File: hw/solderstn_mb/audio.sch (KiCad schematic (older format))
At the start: 28 parts, among them J2103 CES-30207-158L120-67_Molex-Pi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, J2104 CES-703116-28PM_JST-conn, J2105 CES-30207-158L120-67_Molex-Pi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, J2106 CES-703116-28PM_JST-conn, U2102 TS4990IDT, U2103 TS4990IDT

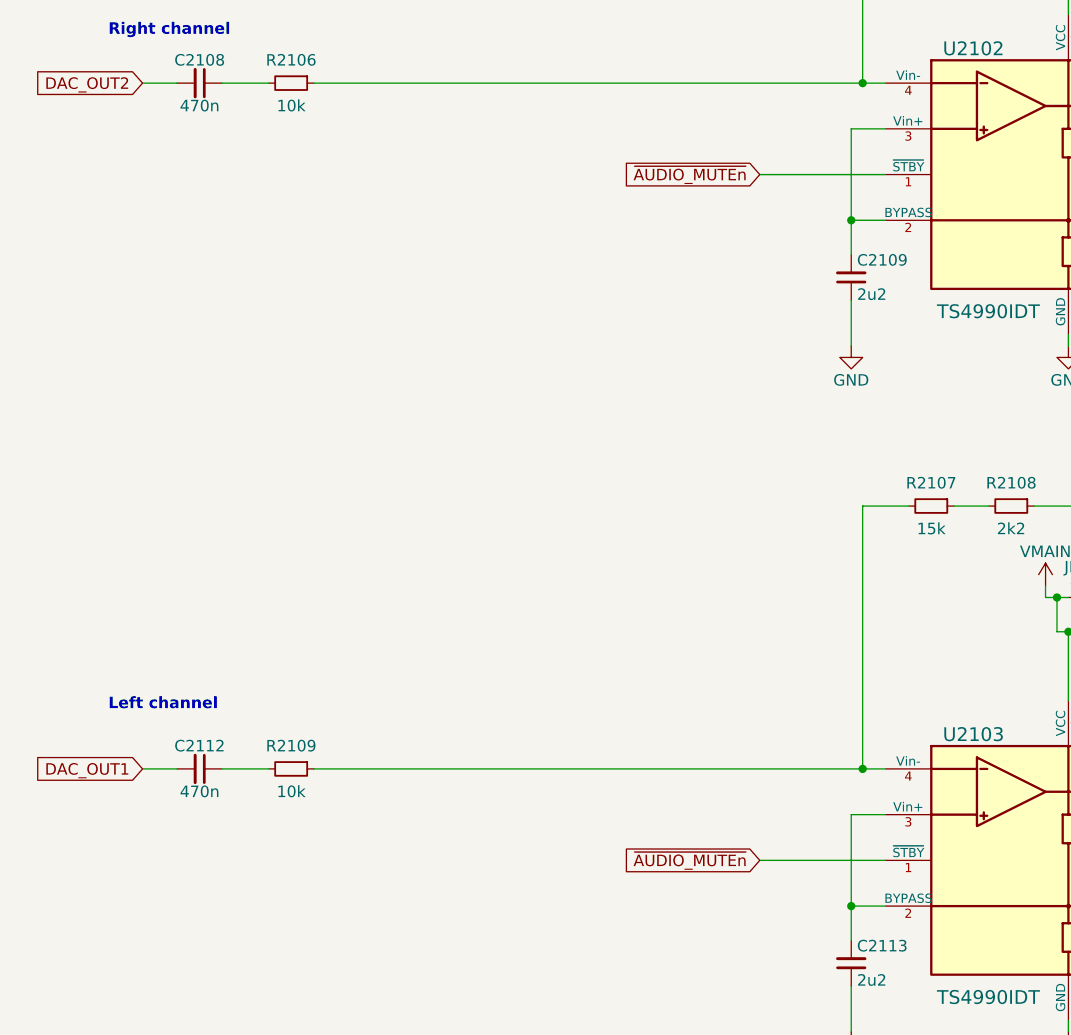
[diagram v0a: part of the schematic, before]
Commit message: MB: 1) remove 2x fan ctrls 2) MCU pin-out for a VS1063 3) add VS1063 DSP/codec to audio path (WIP)
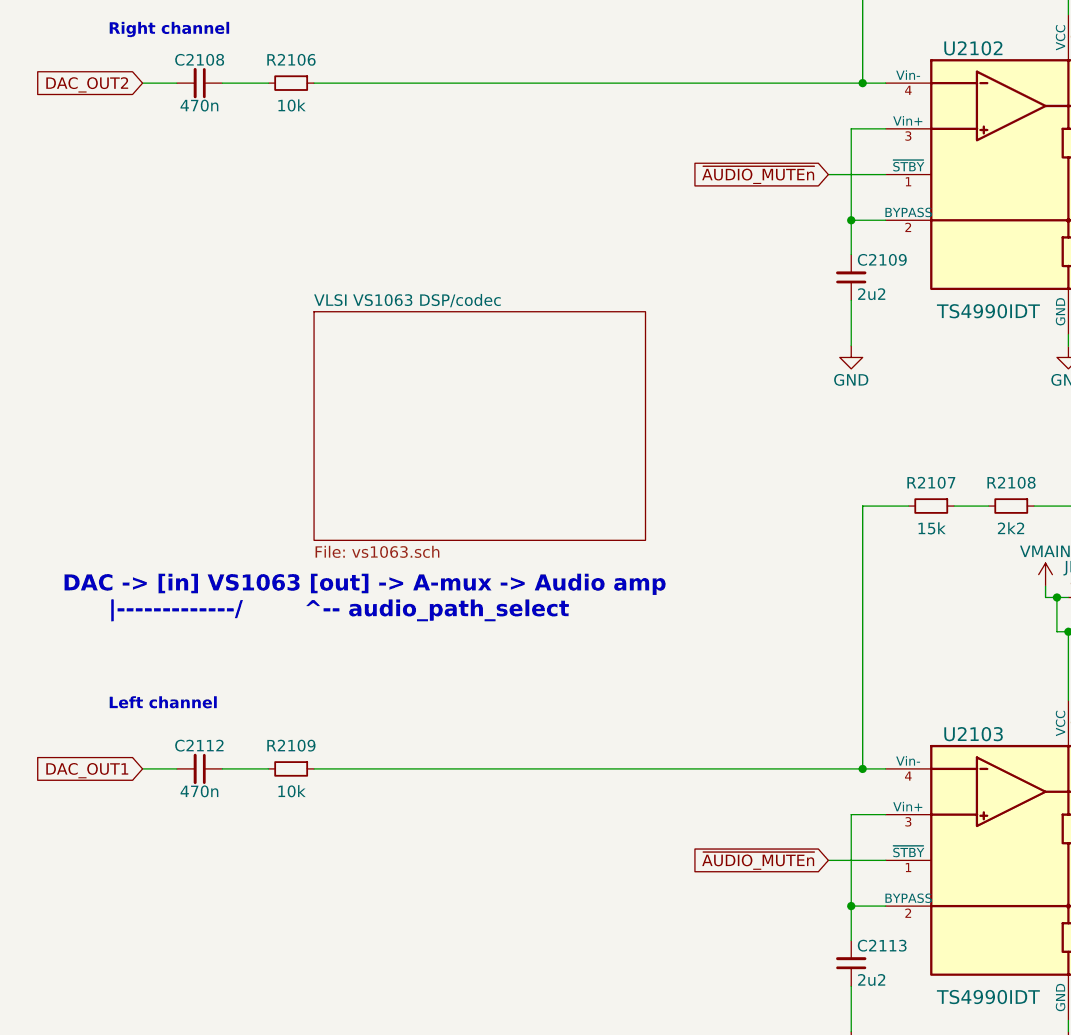
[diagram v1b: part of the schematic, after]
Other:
- note added: "DAC -> [in] VS1063 [out] -> A-mux -> Audio amp\n |-------------/ ^-- audio_path_select"
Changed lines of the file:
@@
 $Descr A4 11693 8268
 encoding utf-8
-Sheet 20 23
+Sheet 20 21
 Title "Audio & MP3/OGG/FLAC :)"
 Date "2020-11-04"
@@
 Connection ~ 4050 2700
 Wire Wire Line
-	4200 2500 3650 2500
-Text GLabel 3650 2500 0    50   Input ~ 0
+	4200 2500 3950 2500
+Text GLabel 3950 2500 0    50   Input ~ 0
 ~AUDIO_MUTEn~
 Text GLabel 950  2100 0    50   Input ~ 0
@@
 Connection ~ 4050 5700
 Wire Wire Line
-	4200 5500 3650 5500
-Text GLabel 3650 5500 0    50   Input ~ 0
+	4200 5500 3950 5500
+Text GLabel 3950 5500 0    50   Input ~ 0
 ~AUDIO_MUTEn~
 Text GLabel 950  5100 0    50   Input ~ 0
@@
 Wire Wire Line
 	4100 3950 4100 5100
+$Sheet
+S 1700 3100 1450 1000
+U 5FEE4431
+F0 "VLSI VS1063 DSP/codec" 50
+F1 "vs1063.sch" 50
+$EndSheet
+Text Notes 600  4450 0    70   ~ 14
+DAC -> [in] VS1063 [out] -> A-mux -> Audio amp\n      |-------------/        ^-- audio_path_select
 $EndSCHEMATC

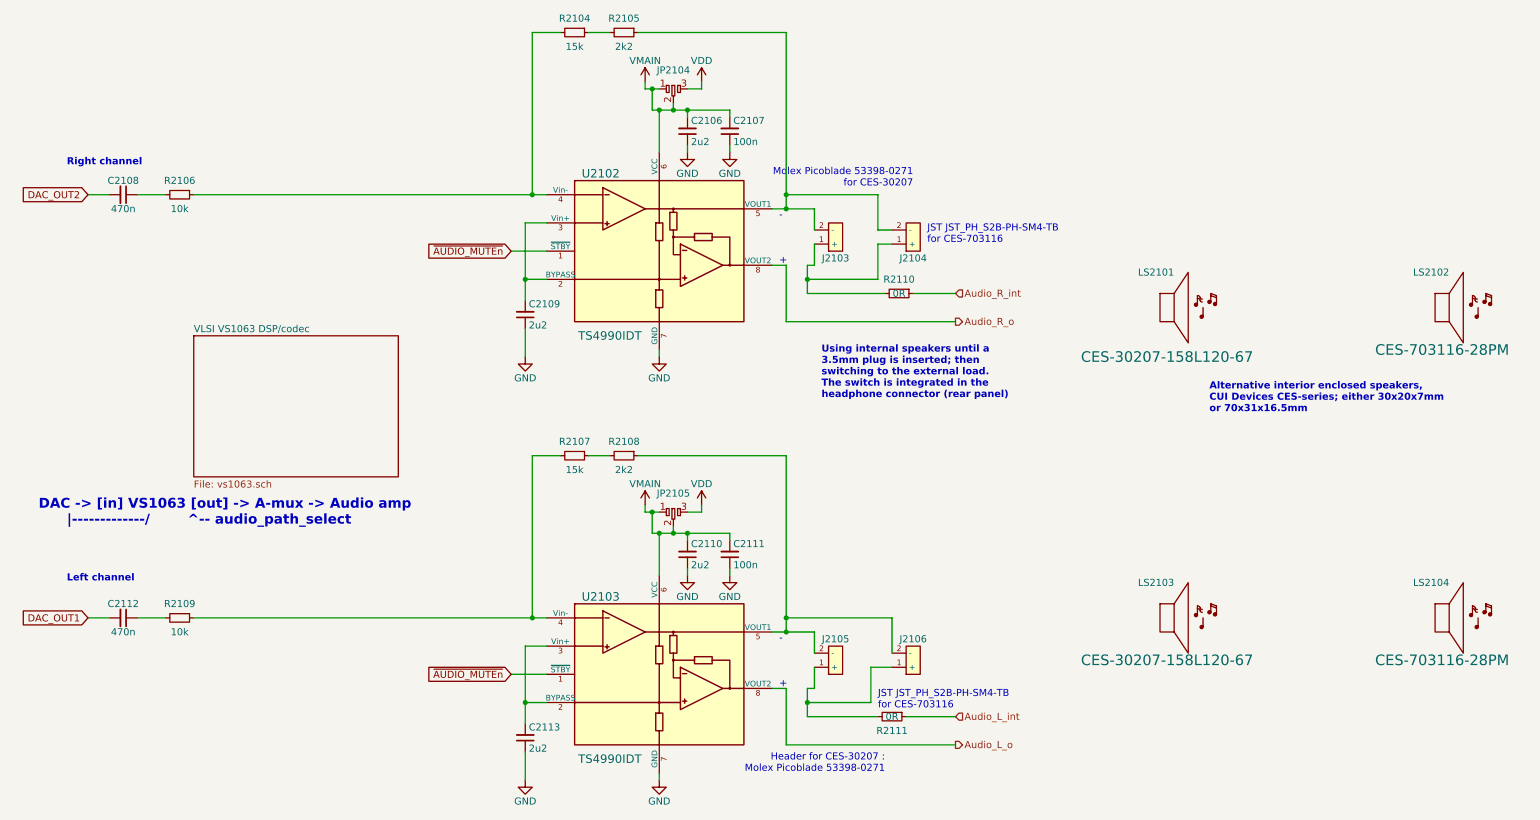
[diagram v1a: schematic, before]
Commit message: MB - Sch design: VS1063 in new audio path; Added: some new ESD, some fixups; Changes: some footprints, fixes
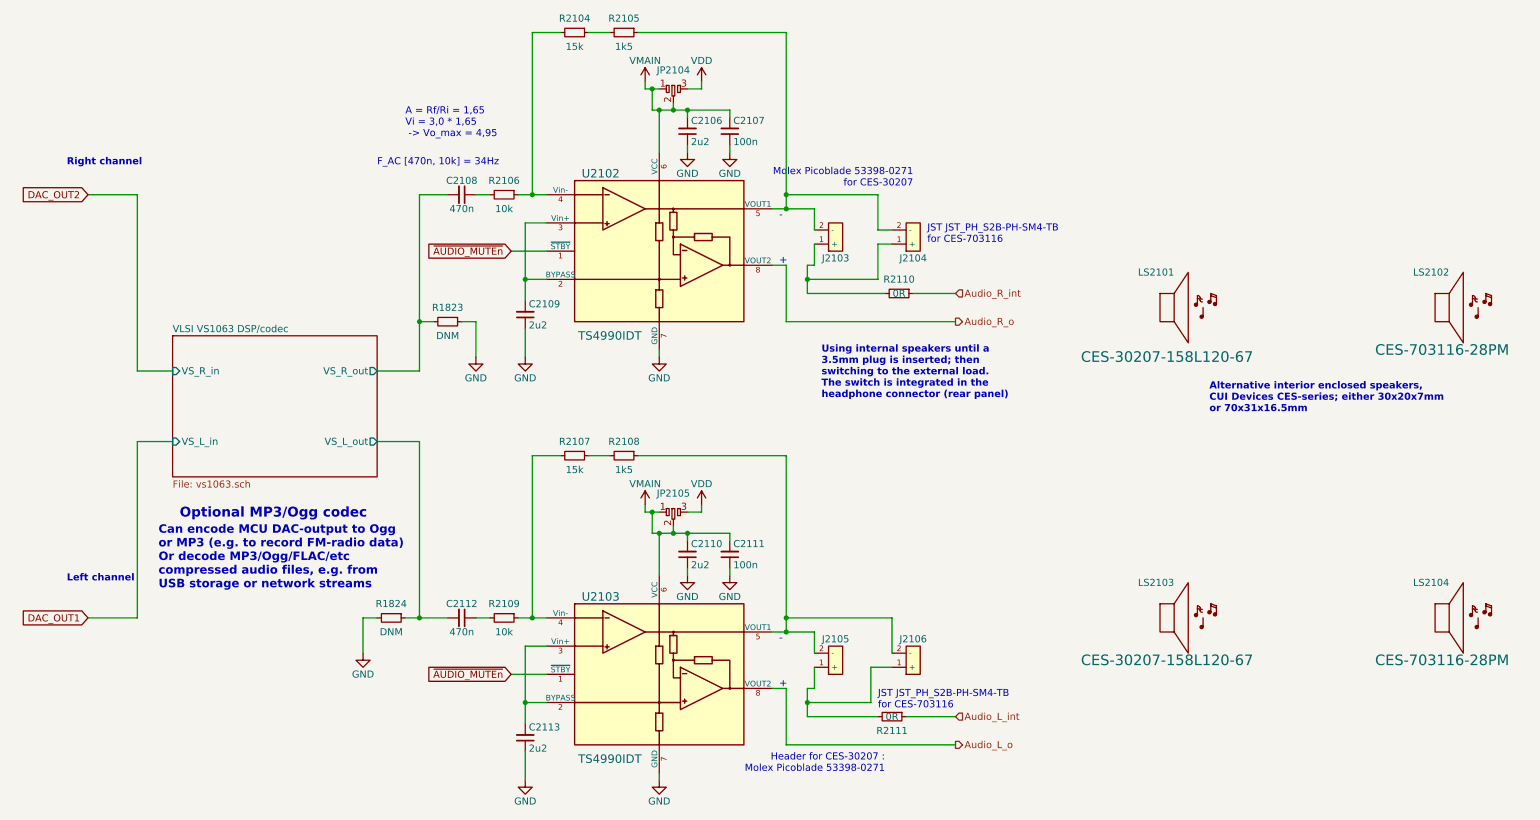
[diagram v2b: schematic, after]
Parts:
- added R1823, R1824: DNM, Resistor_SMD:R_0603_1608Metric, symbol Device:R_Small
- R2105, R2108: value 2k2 -> 1k5
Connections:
- net DAC_OUT1: no longer C2112.2
- net DAC_OUT2: no longer C2108.2
- net GND: now also R1823.1, R1824.2
- new net VLSI VS1063 DSP/codec/VS_L_out: C2112.2, R1824.1
- new net VLSI VS1063 DSP/codec/VS_R_out: C2108.2, R1823.2
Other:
- note added: "A = Rf/Ri = 1,65\nVi = 3,0 * 1,65\n -> Vo_max = 4,95"
- note added: "Can encode MCU DAC-output to Ogg\nor MP3 (e.g. to record FM-radio data)\nOr decode MP3/Ogg/FLAC/etc \ncompressed audio files, e.g. from\nUSB storage or network streams"
- note added: "F_AC [470n, 10k] = 34Hz"
- note added: "Optional MP3/Ogg codec"
- note removed: "DAC -> [in] VS1063 [out] -> A-mux -> Audio amp\n |-------------/ ^-- audio_path_select"
- moved on the sheet: C2108, C2112, R2106, R2109
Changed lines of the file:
@@
 $Descr A4 11693 8268
 encoding utf-8
-Sheet 20 21
+Sheet 18 21
 Title "Audio & MP3/OGG/FLAC :)"
 Date "2020-11-04"
@@
 L Device:C_Small C2108
 U 1 1 5F3BDCEE
-P 1200 2100
-F 0 "C2108" V 1300 2100 50  0000 C CNN
-F 1 "470n" V 1100 2100 50  0000 C CNN
-F 2 "Capacitor_SMD:C_0603_1608Metric" H 1200 2100 50  0001 C CNN
-F 3 "~" H 1200 2100 50  0001 C CNN
-	1    1200 2100
+P 3600 2100
+F 0 "C2108" V 3700 2100 50  0000 C CNN
+F 1 "470n" V 3500 2100 50  0000 C CNN
+F 2 "Capacitor_SMD:C_0603_1608Metric" H 3600 2100 50  0001 C CNN
+F 3 "~" H 3600 2100 50  0001 C CNN
+	1    3600 2100
 	0    1    -1   0
 $EndComp
@@
 P 4750 950
 F 0 "R2105" V 4650 950 50  0000 C CNN
-F 1 "2k2" V 4850 950 50  0000 C CNN
+F 1 "1k5" V 4850 950 50  0000 C CNN
 F 2 "Resistor_SMD:R_0603_1608Metric" H 4750 950 50  0001 C CNN
 F 3 "~" H 4750 950 50  0001 C CNN
@@
 L Device:R_Small R2106
 U 1 1 5F3C4084
-P 1600 2100
-F 0 "R2106" V 1500 2100 50  0000 C CNN
-F 1 "10k" V 1700 2100 50  0000 C CNN
-F 2 "Resistor_SMD:R_0603_1608Metric" H 1600 2100 50  0001 C CNN
-F 3 "~" H 1600 2100 50  0001 C CNN
-	1    1600 2100
+P 3900 2100
+F 0 "R2106" V 3800 2100 50  0000 C CNN
+F 1 "10k" V 4000 2100 50  0000 C CNN
+F 2 "Resistor_SMD:R_0603_1608Metric" H 3900 2100 50  0001 C CNN
+F 3 "~" H 3900 2100 50  0001 C CNN
+	1    3900 2100
 	0    1    1    0
 $EndComp
@@
 	4200 2100 4100 2100
 Wire Wire Line
-	1500 2100 1300 2100
+	3800 2100 3700 2100
 Wire Wire Line
 	4100 950  4100 2100
@@
 	4100 950  4300 950
 Wire Wire Line
-	4100 2100 1700 2100
+	4100 2100 4000 2100
 Wire Wire Line
 	4500 950  4650 950
@@
 DAC_OUT2
 Wire Wire Line
-	950  2100 1100 2100
+	950  2100 1300 2100
 $Comp
 L customlib_mj:TS4990IDT U2103
@@
 L Device:C_Small C2112
 U 1 1 5F416932
-P 1200 5100
-F 0 "C2112" V 1300 5100 50  0000 C CNN
-F 1 "470n" V 1100 5100 50  0000 C CNN
-F 2 "Capacitor_SMD:C_0603_1608Metric" H 1200 5100 50  0001 C CNN
-F 3 "~" H 1200 5100 50  0001 C CNN
-	1    1200 5100
+P 3600 5100
+F 0 "C2112" V 3700 5100 50  0000 C CNN
+F 1 "470n" V 3500 5100 50  0000 C CNN
+F 2 "Capacitor_SMD:C_0603_1608Metric" H 3600 5100 50  0001 C CNN
+F 3 "~" H 3600 5100 50  0001 C CNN
+	1    3600 5100
 	0    1    -1   0
 $EndComp
@@
 P 4750 3950
 F 0 "R2108" V 4650 3950 50  0000 C CNN
-F 1 "2k2" V 4850 3950 50  0000 C CNN
+F 1 "1k5" V 4850 3950 50  0000 C CNN
 F 2 "Resistor_SMD:R_0603_1608Metric" H 4750 3950 50  0001 C CNN
 F 3 "~" H 4750 3950 50  0001 C CNN
@@
 L Device:R_Small R2109
 U 1 1 5F416950
-P 1600 5100
-F 0 "R2109" V 1500 5100 50  0000 C CNN
-F 1 "10k" V 1700 5100 50  0000 C CNN
-F 2 "Resistor_SMD:R_0603_1608Metric" H 1600 5100 50  0001 C CNN
-F 3 "~" H 1600 5100 50  0001 C CNN
-	1    1600 5100
+P 3900 5100
+F 0 "R2109" V 3800 5100 50  0000 C CNN
+F 1 "10k" V 4000 5100 50  0000 C CNN
+F 2 "Resistor_SMD:R_0603_1608Metric" H 3900 5100 50  0001 C CNN
+F 3 "~" H 3900 5100 50  0001 C CNN
+	1    3900 5100
 	0    1    1    0
 $EndComp
@@
 $EndComp
 Wire Wire Line
-	1500 5100 1300 5100
+	3800 5100 3700 5100
 Wire Wire Line
 	4100 3950 4300 3950
@@
 DAC_OUT1
 Wire Wire Line
-	950  5100 1100 5100
+	950  5100 1300 5100
 Wire Wire Line
 	5800 2600 5900 2600
@@
 Audio_L_int
 Wire Wire Line
-	1700 5100 4100 5100
+	4000 5100 4100 5100
 Wire Wire Line
 	4100 5100 4200 5100
@@
 	4100 3950 4100 5100
 $Sheet
-S 1700 3100 1450 1000
+S 1550 3100 1450 1000
 U 5FEE4431
 F0 "VLSI VS1063 DSP/codec" 50
 F1 "vs1063.sch" 50
+F2 "VS_L_in" I L 1550 3850 50
+F3 "VS_R_in" I L 1550 3350 50
+F4 "VS_L_out" O R 3000 3850 50
+F5 "VS_R_out" O R 3000 3350 50
 $EndSheet
-Text Notes 600  4450 0    70   ~ 14
-DAC -> [in] VS1063 [out] -> A-mux -> Audio amp\n      |-------------/        ^-- audio_path_select
+Text Notes 1600 4400 0    70   ~ 14
+Optional MP3/Ogg codec
+Wire Wire Line
+	1550 3350 1300 3350
+Wire Wire Line
+	1300 3350 1300 2100
+Wire Wire Line
+	1550 3850 1300 3850
+Wire Wire Line
+	1300 3850 1300 5100
+Wire Wire Line
+	3000 3350 3300 3350
+Wire Wire Line
+	3300 2100 3500 2100
+Wire Wire Line
+	3000 3850 3300 3850
+Wire Wire Line
+	3300 3850 3300 5100
+Wire Wire Line
+	3300 5100 3500 5100
+Text Notes 1450 4900 0    60   ~ 12
+Can encode MCU DAC-output to Ogg\nor MP3 (e.g. to record FM-radio data)\nOr decode MP3/Ogg/FLAC/etc \ncompressed audio files, e.g. from\nUSB storage or network streams
+Text Notes 3000 1900 0    50   ~ 0
+F_AC [470n, 10k] = 34Hz
+Text Notes 3200 1700 0    50   ~ 0
+A = Rf/Ri = 1,65\nVi = 3,0 * 1,65\n -> Vo_max = 4,95
+$Comp
+L power:GND #PWR01840
+U 1 1 603DF358
+P 3700 3250
+F 0 "#PWR01840" H 3700 3000 50  0001 C CNN
+F 1 "GND" H 3700 3100 50  0000 C CNN
+F 2 "" H 3700 3250 50  0001 C CNN
+F 3 "" H 3700 3250 50  0001 C CNN
+	1    3700 3250
+	1    0    0    -1
+$EndComp
+$Comp
+L Device:R_Small R1823
+U 1 1 603DFCE1
+P 3500 3000
+F 0 "R1823" V 3400 3000 50  0000 C CNN
+F 1 "DNM" V 3600 3000 50  0000 C CNN
+F 2 "Resistor_SMD:R_0603_1608Metric" H 3500 3000 50  0001 C CNN
+F 3 "~" H 3500 3000 50  0001 C CNN
+	1    3500 3000
+	0    1    1    0
+$EndComp
+Wire Wire Line
+	3600 3000 3700 3000
+Wire Wire Line
+	3700 3000 3700 3250
+Wire Wire Line
+	3300 2100 3300 3000
+Wire Wire Line
+	3400 3000 3300 3000
+Connection ~ 3300 3000
+Wire Wire Line
+	3300 3000 3300 3350
+$Comp
+L power:GND #PWR01841
+U 1 1 603F2EB2
+P 2900 5350
+F 0 "#PWR01841" H 2900 5100 50  0001 C CNN
+F 1 "GND" H 2900 5200 50  0000 C CNN
+F 2 "" H 2900 5350 50  0001 C CNN
+F 3 "" H 2900 5350 50  0001 C CNN
+	1    2900 5350
+	1    0    0    -1
+$EndComp
+$Comp
+L Device:R_Small R1824
+U 1 1 603F3260
+P 3100 5100
+F 0 "R1824" V 3000 5100 50  0000 C CNN
+F 1 "DNM" V 3200 5100 50  0000 C CNN
+F 2 "Resistor_SMD:R_0603_1608Metric" H 3100 5100 50  0001 C CNN
+F 3 "~" H 3100 5100 50  0001 C CNN
+	1    3100 5100
+	0    1    1    0
+$EndComp
+Wire Wire Line
+	2900 5100 2900 5350
+Wire Wire Line
+	3200 5100 3300 5100
+Connection ~ 3300 5100
+Wire Wire Line
+	3000 5100 2900 5100
 $EndSCHEMATC
